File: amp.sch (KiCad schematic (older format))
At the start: 26 parts, among them IC1 STM32F103CBU6, IC2 MCP1700, J1 SERIAL, J2 MICROUSB, P1 SWD_TC, P2 SWD, Q1 PFET, Y1 8MHz

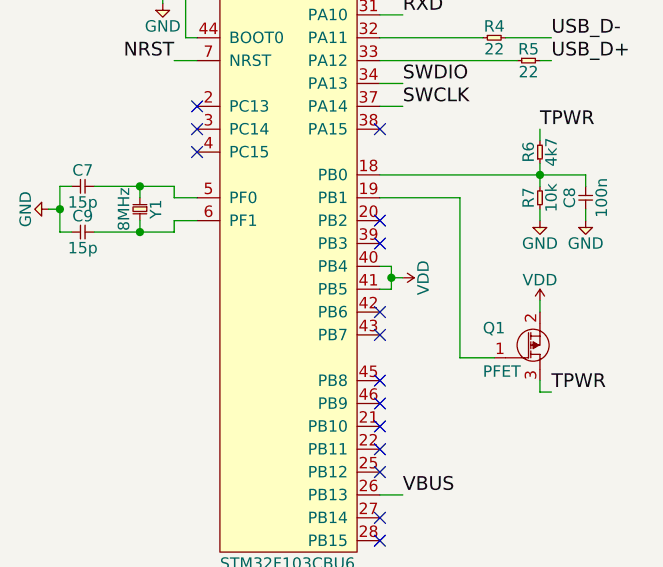
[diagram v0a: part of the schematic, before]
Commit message: Only need PB5 for version sensing
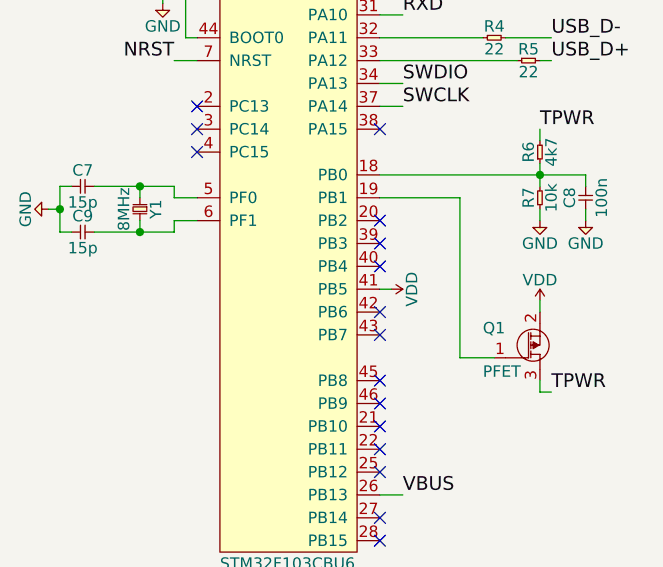
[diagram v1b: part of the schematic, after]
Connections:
- net VDD: no longer IC1.40 (PB4)
- no-connect marks 21 -> 22
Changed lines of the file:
@@
 L VDD #PWR017
 U 1 1 5686983C
-P 3650 4800
-F 0 "#PWR017" H 3650 4910 50  0001 L CNN
-F 1 "VDD" H 3650 4890 50  0000 C CNN
-F 2 "" H 3650 4800 60  0000 C CNN
-F 3 "" H 3650 4800 60  0000 C CNN
-	1    3650 4800
+P 3600 4850
+F 0 "#PWR017" H 3600 4960 50  0001 L CNN
+F 1 "VDD" H 3600 4940 50  0000 C CNN
+F 2 "" H 3600 4850 60  0000 C CNN
+F 3 "" H 3600 4850 60  0000 C CNN
+	1    3600 4850
 	0    1    1    0
 $EndComp
@@
 	3550 4450 3900 4450
 Wire Wire Line
-	3550 4750 3600 4750
-Wire Wire Line
-	3600 4750 3600 4850
-Wire Wire Line
 	3600 4850 3550 4850
-Wire Wire Line
-	3600 4800 3650 4800
-Connection ~ 3600 4800
 Wire Wire Line
 	3250 700  3250 750
@@
 	4250 1700 4250 1650
 Connection ~ 4150 1700
+NoConn ~ 3550 4750
 $EndSCHEMATC

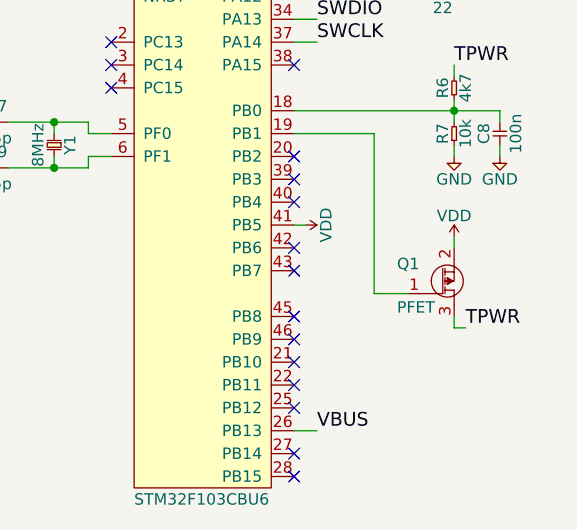
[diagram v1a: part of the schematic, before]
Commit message: Specify the PFET
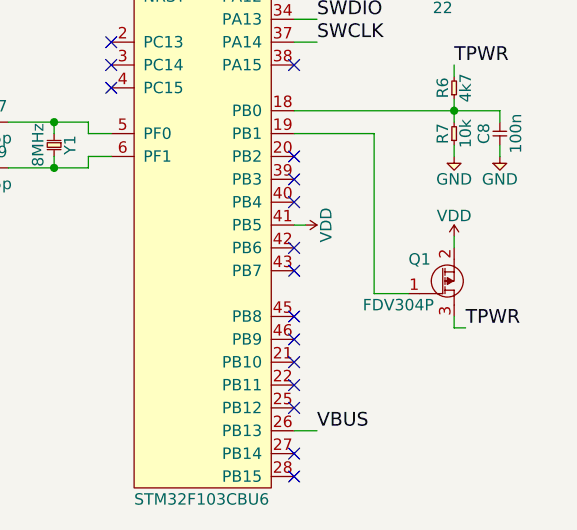
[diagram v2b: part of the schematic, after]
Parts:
- Q1: value PFET -> FDV304P; footprint (none) -> agg:SOT-23; Farnell (none) -> 9846123
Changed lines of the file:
@@
 U 1 1 56864DEA
 P 4250 5050
-F 0 "Q1" H 4000 5080 50  0000 L CNN
-F 1 "PFET" H 4000 4890 50  0000 L CNN
-F 2 "" H 4250 5050 60  0000 C CNN
+F 0 "Q1" H 4050 5100 50  0000 L CNN
+F 1 "FDV304P" H 3850 4900 50  0000 L CNN
+F 2 "agg:SOT-23" H 4250 5050 60  0001 C CNN
 F 3 "" H 4250 5050 60  0000 C CNN
+F 4 "9846123" H 4250 5050 60  0001 C CNN "Farnell"
 	1    4250 5050
 	1    0    0    -1

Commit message: mostly routed go
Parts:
- C1, C10, C11, C2: footprint agg:0603N -> agg:0603
- C3, C4, C5, C6, C8: footprint agg:0402N -> agg:0402
- C7, C9, R1, R2, R3, R4, R5, R6, R7: footprint (none) -> agg:0402
- IC1: Farnell (none) -> 2060891; Field4 2060891 -> (none)
- J1: footprint (none) -> agg:SM04B-PASS
- Y1: footprint (none) -> agg:XTAL-50x32; Farnell (none) -> 2101329
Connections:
- net GND: now also C1.1, C2.1, C3.1, C4.1, C5.1, C6.1
- net VDD: no longer C1.1, C2.1, C3.1, C4.1, C5.1, C6.1
- net STM32_D-: now reaches IC1.32 (PA11), R4.1
- net STM32_D+: now reaches IC1.33 (PA12), R5.1
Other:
- moved on the sheet: C1, C2, C3, C4, C5, C6
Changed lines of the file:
@@
 F 2 "agg:QFN-48-EP-ST" H 2850 2350 50  0001 L CNN
 F 3 "http://www.st.com/st-web-ui/static/active/en/resource/technical/document/datasheet/CD00161566.pdf" H 2850 2250 50  0001 L CNN
-F 4 "2060891" H 2850 2150 50  0001 L CNN "Field4"
+F 4 "2060891" H 3150 4250 60  0001 C CNN "Farnell"
 	1    3150 4250
 	1    0    0    -1
@@
 F 0 "J1" H 2350 650 50  0000 L CNN
 F 1 "SERIAL" V 2300 900 50  0000 C CNN
-F 2 "" H 2400 1050 60  0000 C CNN
+F 2 "agg:SM04B-PASS" H 2400 1050 60  0001 C CNN
 F 3 "" H 2400 1050 60  0000 C CNN
 	1    2400 1050
@@
 F 0 "R4" H 4050 3800 50  0000 C CNN
 F 1 "22" H 4050 3700 50  0000 C CNN
-F 2 "" H 4000 3750 60  0000 C CNN
+F 2 "agg:0402" H 4000 3750 60  0001 C CNN
 F 3 "" H 4000 3750 60  0000 C CNN
 	1    4000 3750
@@
 F 0 "R5" H 4200 3900 50  0000 C CNN
 F 1 "22" H 4200 3800 50  0000 C CNN
-F 2 "" H 4150 3850 60  0000 C CNN
+F 2 "agg:0402" H 4150 3850 60  0001 C CNN
 F 3 "" H 4150 3850 60  0000 C CNN
 	1    4150 3850
@@
 F 0 "R3" H 4100 3500 50  0000 C CNN
 F 1 "1k5" H 4100 3400 50  0000 C CNN
-F 2 "" H 4050 3450 60  0000 C CNN
+F 2 "agg:0402" H 4050 3450 60  0001 C CNN
 F 3 "" H 4050 3450 60  0000 C CNN
 	1    4050 3450
@@
 F 0 "R1" H 2200 1600 50  0000 C CNN
 F 1 "4k7" H 2200 1500 50  0000 C CNN
-F 2 "" H 2150 1550 60  0000 C CNN
+F 2 "agg:0402" H 2150 1550 60  0001 C CNN
 F 3 "" H 2150 1550 60  0000 C CNN
 	1    2150 1550
@@
 F 0 "R2" H 2200 1800 50  0000 C CNN
 F 1 "10k" H 2200 1700 50  0000 C CNN
-F 2 "" H 2150 1750 60  0000 C CNN
+F 2 "agg:0402" H 2150 1750 60  0001 C CNN
 F 3 "" H 2150 1750 60  0000 C CNN
 	1    2150 1750
@@
 F 0 "Y1" H 2550 4520 50  0000 C CNN
 F 1 "8MHz" H 2550 4380 50  0000 C CNN
-F 2 "" H 2500 4450 60  0000 C CNN
+F 2 "agg:XTAL-50x32" H 2500 4450 60  0001 C CNN
 F 3 "" H 2500 4450 60  0000 C CNN
+F 4 "2101329" H 2500 4450 50  0001 L CNN "Farnell"
 	1    2500 4450
 	0    1    1    0
@@
 F 0 "C7" H 2250 4470 50  0000 C CNN
 F 1 "15p" H 2250 4330 50  0000 C CNN
-F 2 "" H 2200 4400 60  0000 C CNN
+F 2 "agg:0402" H 2200 4400 60  0001 C CNN
 F 3 "" H 2200 4400 60  0000 C CNN
 	1    2200 4400
@@
 F 0 "C9" H 2250 4670 50  0000 C CNN
 F 1 "15p" H 2250 4530 50  0000 C CNN
-F 2 "" H 2200 4600 60  0000 C CNN
+F 2 "agg:0402" H 2200 4600 60  0001 C CNN
 F 3 "" H 2200 4600 60  0000 C CNN
 	1    2200 4600
@@
 L C C5
 U 1 1 56866C90
-P 2250 2750
-F 0 "C5" H 2300 2820 50  0000 C CNN
-F 1 "100n" H 2300 2680 50  0000 C CNN
-F 2 "agg:0402N" H 2250 2750 60  0001 C CNN
-F 3 "" H 2250 2750 60  0000 C CNN
-	1    2250 2750
+P 2150 3000
+F 0 "C5" H 2200 3070 50  0000 C CNN
+F 1 "100n" H 2200 2930 50  0000 C CNN
+F 2 "agg:0402" H 2150 3000 60  0001 C CNN
+F 3 "" H 2150 3000 60  0000 C CNN
+	1    2150 3000
 	0    -1   -1   0
 $EndComp
@@
 L C C4
 U 1 1 56866F6D
-P 2000 2750
-F 0 "C4" H 2050 2820 50  0000 C CNN
-F 1 "100n" H 2050 2680 50  0000 C CNN
-F 2 "agg:0402N" H 2000 2750 60  0001 C CNN
-F 3 "" H 2000 2750 60  0000 C CNN
-	1    2000 2750
+P 1900 2900
+F 0 "C4" H 1950 2970 50  0000 C CNN
+F 1 "100n" H 1950 2830 50  0000 C CNN
+F 2 "agg:0402" H 1900 2900 60  0001 C CNN
+F 3 "" H 1900 2900 60  0000 C CNN
+	1    1900 2900
 	0    -1   -1   0
 $EndComp
@@
 L C C3
 U 1 1 56866FB0
-P 1750 2750
-F 0 "C3" H 1800 2820 50  0000 C CNN
-F 1 "100n" H 1800 2680 50  0000 C CNN
-F 2 "agg:0402N" H 1750 2750 60  0001 C CNN
-F 3 "" H 1750 2750 60  0000 C CNN
-	1    1750 2750
+P 1650 2800
+F 0 "C3" H 1700 2870 50  0000 C CNN
+F 1 "100n" H 1700 2730 50  0000 C CNN
+F 2 "agg:0402" H 1650 2800 60  0001 C CNN
+F 3 "" H 1650 2800 60  0000 C CNN
+	1    1650 2800
 	0    -1   -1   0
 $EndComp
@@
 L C C6
 U 1 1 56867348
-P 2500 2750
-F 0 "C6" H 2550 2820 50  0000 C CNN
-F 1 "10n" H 2550 2680 50  0000 C CNN
-F 2 "agg:0402N" H 2500 2750 60  0001 C CNN
-F 3 "" H 2500 2750 60  0000 C CNN
-	1    2500 2750
+P 2600 3100
+F 0 "C6" H 2650 3170 50  0000 C CNN
+F 1 "10n" H 2650 3030 50  0000 C CNN
+F 2 "agg:0402" H 2600 3100 60  0001 C CNN
+F 3 "" H 2600 3100 60  0000 C CNN
+	1    2600 3100
 	0    -1   -1   0
 $EndComp
@@
 L C C2
 U 1 1 568673BC
-P 1500 2750
-F 0 "C2" H 1550 2800 50  0000 C CNN
-F 1 "1µ" H 1550 2680 50  0000 C CNN
-F 2 "agg:0603N" H 1500 2750 60  0001 C CNN
-F 3 "" H 1500 2750 60  0000 C CNN
-	1    1500 2750
+P 2350 3100
+F 0 "C2" H 2400 3150 50  0000 C CNN
+F 1 "1µ" H 2400 3030 50  0000 C CNN
+F 2 "agg:0603" H 2350 3100 60  0001 C CNN
+F 3 "" H 2350 3100 60  0000 C CNN
+	1    2350 3100
 	0    -1   -1   0
 $EndComp
@@
 L C C1
 U 1 1 5686747A
-P 1250 2750
-F 0 "C1" H 1300 2820 50  0000 C CNN
-F 1 "4µ7" H 1300 2680 50  0000 C CNN
-F 2 "agg:0603N" H 1250 2750 60  0001 C CNN
-F 3 "" H 1250 2750 60  0000 C CNN
-	1    1250 2750
+P 1400 2800
+F 0 "C1" H 1450 2870 50  0000 C CNN
+F 1 "4µ7" H 1450 2730 50  0000 C CNN
+F 2 "agg:0603" H 1400 2800 60  0001 C CNN
+F 3 "" H 1400 2800 60  0000 C CNN
+	1    1400 2800
 	0    -1   -1   0
 $EndComp
@@
 F 0 "R6" H 4300 4350 50  0000 C CNN
 F 1 "4k7" H 4300 4250 50  0000 C CNN
-F 2 "" H 4250 4300 60  0000 C CNN
+F 2 "agg:0402" H 4250 4300 60  0001 C CNN
 F 3 "" H 4250 4300 60  0000 C CNN
 	1    4250 4300
@@
 F 0 "R7" H 4300 4550 50  0000 C CNN
 F 1 "10k" H 4300 4450 50  0000 C CNN
-F 2 "" H 4250 4500 60  0000 C CNN
+F 2 "agg:0402" H 4250 4500 60  0001 C CNN
 F 3 "" H 4250 4500 60  0000 C CNN
 	1    4250 4500
@@
 F 0 "C8" H 4500 4570 50  0000 C CNN
 F 1 "100n" H 4500 4430 50  0000 C CNN
-F 2 "agg:0402N" H 4450 4500 60  0001 C CNN
+F 2 "agg:0402" H 4450 4500 60  0001 C CNN
 F 3 "" H 4450 4500 60  0000 C CNN
 	1    4450 4500
@@
 F 0 "C11" H 4200 1920 50  0000 C CNN
 F 1 "1µ" H 4200 1780 50  0000 C CNN
-F 2 "agg:0603N" H 4150 1850 60  0001 C CNN
+F 2 "agg:0603" H 4150 1850 60  0001 C CNN
 F 3 "" H 4150 1850 60  0000 C CNN
 	1    4150 1850
@@
 F 0 "C10" H 3100 1920 50  0000 C CNN
 F 1 "1µ" H 3100 1780 50  0000 C CNN
-F 2 "agg:0603N" H 3050 1850 60  0001 C CNN
+F 2 "agg:0603" H 3050 1850 60  0001 C CNN
 F 3 "" H 3050 1850 60  0000 C CNN
 	1    3050 1850
 	0    -1   -1   0
 $EndComp
+NoConn ~ 3550 4750
 Wire Wire Line
 	3550 3950 3650 3950
@@
 	2650 3850 2750 3850
 Wire Wire Line
-	2750 3150 2600 3150
-Wire Wire Line
-	2600 3150 2600 3600
-Wire Wire Line
-	2750 3250 2600 3250
+	2600 3100 2600 3600
+Wire Wire Line
+	1400 3250 2750 3250
 Connection ~ 2600 3250
 Wire Wire Line
-	2750 3350 2600 3350
+	1900 3350 2750 3350
 Connection ~ 2600 3350
 Wire Wire Line
-	2750 3450 2600 3450
+	2150 3450 2750 3450
 Connection ~ 2600 3450
 Wire Wire Line
@@
 Wire Wire Line
 	2700 2500 2700 2950
-Wire Wire Line
-	1250 2950 2750 2950
-Wire Wire Line
-	2750 2850 2700 2850
 Connection ~ 2700 2850
-Wire Wire Line
-	2750 2750 2700 2750
 Connection ~ 2700 2750
 Wire Wire Line
-	2750 2650 2700 2650
+	1400 2650 2750 2650
 Connection ~ 2700 2650
-Wire Wire Line
-	1250 2550 2750 2550
 Connection ~ 2700 2550
-Wire Wire Line
-	2500 2750 2500 2950
-Connection ~ 2700 2950
-Wire Wire Line
-	1250 2950 1250 2750
-Connection ~ 2500 2950
-Wire Wire Line
-	1500 2750 1500 2950
-Connection ~ 1500 2950
-Wire Wire Line
-	1750 2750 1750 2950
-Connection ~ 1750 2950
-Wire Wire Line
-	2000 2750 2000 2950
-Connection ~ 2000 2950
-Wire Wire Line
-	2250 2750 2250 2950
-Connection ~ 2250 2950
-Wire Wire Line
-	1250 2650 1250 2550
-Wire Wire Line
-	2500 2650 2500 2550
-Connection ~ 2500 2550
-Wire Wire Line
-	2250 2650 2250 2550
-Connection ~ 2250 2550
-Wire Wire Line
-	2000 2650 2000 2550
-Connection ~ 2000 2550
-Wire Wire Line
-	1750 2650 1750 2550
-Connection ~ 1750 2550
-Wire Wire Line
-	1500 2650 1500 2550
-Connection ~ 1500 2550
 Wire Wire Line
 	4400 1150 4300 1150
@@
 	4250 1700 4250 1650
 Connection ~ 4150 1700
-NoConn ~ 3550 4750
+Wire Wire Line
+	2350 2950 2750 2950
+Wire Wire Line
+	2350 3150 2750 3150
+Wire Wire Line
+	2750 2550 2700 2550
+Wire Wire Line
+	2600 2950 2600 3000
+Connection ~ 2700 2950
+Wire Wire Line
+	2350 2950 2350 3000
+Connection ~ 2600 2950
+Connection ~ 2600 3150
+Wire Wire Line
+	2350 3100 2350 3150
+Wire Wire Line
+	1650 2650 1650 2700
+Wire Wire Line
+	1400 2650 1400 2700
+Connection ~ 1650 2650
+Wire Wire Line
+	2750 2850 2150 2850
+Wire Wire Line
+	2150 2850 2150 2900
+Wire Wire Line
+	2750 2750 1900 2750
+Wire Wire Line
+	1900 2750 1900 2800
+Wire Wire Line
+	2150 3000 2150 3450
+Wire Wire Line
+	1900 2900 1900 3350
+Wire Wire Line
+	1650 2800 1650 3250
+Wire Wire Line
+	1400 2800 1400 3250
+Connection ~ 1650 3250
+Text Label 3550 3750 0    30   ~ 0
+STM32_D-
+Text Label 3550 3850 0    30   ~ 0
+STM32_D+
 $EndSCHEMATC

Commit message: fully routed
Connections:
- net GND: now also J1.4; no longer J1.1
- net RXD: now also J1.3; no longer J1.2
- net TXD: now also J1.2; no longer J1.3
- net VDD: now also J1.1; no longer J1.4
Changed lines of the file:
@@
 L CONN_01x04 J1
 U 1 1 568643A2
-P 2400 1050
-F 0 "J1" H 2350 650 50  0000 L CNN
-F 1 "SERIAL" V 2300 900 50  0000 C CNN
-F 2 "agg:SM04B-PASS" H 2400 1050 60  0001 C CNN
-F 3 "" H 2400 1050 60  0000 C CNN
-	1    2400 1050
-	1    0    0    1
+P 2400 750
+F 0 "J1" H 2350 350 50  0000 L CNN
+F 1 "SERIAL" V 2300 600 50  0000 C CNN
+F 2 "agg:SM04B-PASS" H 2400 750 60  0001 C CNN
+F 3 "" H 2400 750 60  0000 C CNN
+	1    2400 750
+	1    0    0    -1
 $EndComp
 Text Label 3650 3950 0    60   ~ 0

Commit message: try swap to surface-mount swd connector
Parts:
- P2: footprint agg:FTSH-105-01-F-D-K -> agg:FTSH-105-01-L-DV-K; Toby FTSH-105-01-F-D-K -> agg:FTSH-105-01-L-DV-K
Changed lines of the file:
@@
 F 0 "P2" H 3400 1250 50  0000 L CNN
 F 1 "SWD" H 3400 650 50  0000 L CNN
-F 2 "agg:FTSH-105-01-F-D-K" H 3400 550 50  0001 L CNN
+F 2 "agg:FTSH-105-01-L-DV-K" H 3400 550 50  0001 L CNN
 F 3 "" H 4150 750 50  0000 C CNN
-F 4 "FTSH-105-01-F-D-K" H 3400 450 50  0001 L CNN "Toby"
+F 4 "agg:FTSH-105-01-L-DV-K" H 3400 450 50  0001 L CNN "Toby"
 	1    3800 950
 	1    0    0    -1

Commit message: Add Farnell order codes
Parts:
- C1: Farnell (none) -> 2496930
- C10, C11, C2: Farnell (none) -> 2496916
- C3, C4, C5, C8: Farnell (none) -> 1759380
- C6: Farnell (none) -> 1758924
- C7, C9: value 15p -> 33p; Farnell (none) -> 1758955
- J1: Farnell (none) -> 2399347
- P2: Toby agg:FTSH-105-01-L-DV-K -> FTSH-105-01-L-DV-K
- R1, R6: Farnell (none) -> 2447187
- R2, R7: Farnell (none) -> 2447096
- R3: Farnell (none) -> 2447125
- R4, R5: Farnell (none) -> 2447138
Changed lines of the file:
@@
 F 2 "agg:FTSH-105-01-L-DV-K" H 3400 550 50  0001 L CNN
 F 3 "" H 4150 750 50  0000 C CNN
-F 4 "agg:FTSH-105-01-L-DV-K" H 3400 450 50  0001 L CNN "Toby"
+F 4 "FTSH-105-01-L-DV-K" H 3400 450 50  0001 L CNN "Toby"
 	1    3800 950
 	1    0    0    -1
@@
 F 2 "agg:SM04B-PASS" H 2400 750 60  0001 C CNN
 F 3 "" H 2400 750 60  0000 C CNN
+F 4 "2399347" H 2400 750 60  0001 C CNN "Farnell"
 	1    2400 750
 	1    0    0    -1
@@
 F 2 "agg:0402" H 4000 3750 60  0001 C CNN
 F 3 "" H 4000 3750 60  0000 C CNN
+F 4 "2447138" H 4000 3750 60  0001 C CNN "Farnell"
 	1    4000 3750
 	1    0    0    -1
@@
 F 2 "agg:0402" H 4150 3850 60  0001 C CNN
 F 3 "" H 4150 3850 60  0000 C CNN
+F 4 "2447138" H 4150 3850 60  0001 C CNN "Farnell"
 	1    4150 3850
 	1    0    0    -1
@@
 F 2 "agg:0402" H 4050 3450 60  0001 C CNN
 F 3 "" H 4050 3450 60  0000 C CNN
+F 4 "2447125" H 4050 3450 60  0001 C CNN "Farnell"
 	1    4050 3450
 	1    0    0    -1
@@
 F 2 "agg:0402" H 2150 1550 60  0001 C CNN
 F 3 "" H 2150 1550 60  0000 C CNN
+F 4 "2447187" H 2150 1550 60  0001 C CNN "Farnell"
 	1    2150 1550
 	0    -1   -1   0
@@
 F 2 "agg:0402" H 2150 1750 60  0001 C CNN
 F 3 "" H 2150 1750 60  0000 C CNN
+F 4 "2447096" H 2150 1750 60  0001 C CNN "Farnell"
 	1    2150 1750
 	0    -1   -1   0
@@
 P 2200 4400
 F 0 "C7" H 2250 4470 50  0000 C CNN
-F 1 "15p" H 2250 4330 50  0000 C CNN
+F 1 "33p" H 2250 4330 50  0000 C CNN
 F 2 "agg:0402" H 2200 4400 60  0001 C CNN
 F 3 "" H 2200 4400 60  0000 C CNN
+F 4 "1758955" H 2200 4400 60  0001 C CNN "Farnell"
 	1    2200 4400
 	1    0    0    -1
@@
 P 2200 4600
 F 0 "C9" H 2250 4670 50  0000 C CNN
-F 1 "15p" H 2250 4530 50  0000 C CNN
+F 1 "33p" H 2250 4530 50  0000 C CNN
 F 2 "agg:0402" H 2200 4600 60  0001 C CNN
 F 3 "" H 2200 4600 60  0000 C CNN
+F 4 "1758955" H 2200 4600 60  0001 C CNN "Farnell"
 	1    2200 4600
 	1    0    0    -1
@@
 F 2 "agg:0402" H 2150 3000 60  0001 C CNN
 F 3 "" H 2150 3000 60  0000 C CNN
+F 4 "1759380" H 2150 3000 60  0001 C CNN "Farnell"
 	1    2150 3000
 	0    -1   -1   0
@@
 F 2 "agg:0402" H 1900 2900 60  0001 C CNN
 F 3 "" H 1900 2900 60  0000 C CNN
+F 4 "1759380" H 1900 2900 60  0001 C CNN "Farnell"
 	1    1900 2900
 	0    -1   -1   0
@@
 F 2 "agg:0402" H 1650 2800 60  0001 C CNN
 F 3 "" H 1650 2800 60  0000 C CNN
+F 4 "1759380" H 1650 2800 60  0001 C CNN "Farnell"
 	1    1650 2800
 	0    -1   -1   0
@@
 F 2 "agg:0402" H 2600 3100 60  0001 C CNN
 F 3 "" H 2600 3100 60  0000 C CNN
+F 4 "1758924" H 2600 3100 60  0001 C CNN "Farnell"
 	1    2600 3100
 	0    -1   -1   0
@@
 F 2 "agg:0603" H 2350 3100 60  0001 C CNN
 F 3 "" H 2350 3100 60  0000 C CNN
+F 4 "2496916" H 2350 3100 60  0001 C CNN "Farnell"
 	1    2350 3100
 	0    -1   -1   0
@@
 F 2 "agg:0603" H 1400 2800 60  0001 C CNN
 F 3 "" H 1400 2800 60  0000 C CNN
+F 4 "2496930" H 1400 2800 60  0001 C CNN "Farnell"
 	1    1400 2800
 	0    -1   -1   0
@@
 F 2 "agg:0402" H 4250 4300 60  0001 C CNN
 F 3 "" H 4250 4300 60  0000 C CNN
+F 4 "2447187" H 4250 4300 60  0001 C CNN "Farnell"
 	1    4250 4300
 	0    -1   -1   0
@@
 F 2 "agg:0402" H 4250 4500 60  0001 C CNN
 F 3 "" H 4250 4500 60  0000 C CNN
+F 4 "2447096" H 4250 4500 60  0001 C CNN "Farnell"
 	1    4250 4500
 	0    -1   -1   0
@@
 F 2 "agg:0402" H 4450 4500 60  0001 C CNN
 F 3 "" H 4450 4500 60  0000 C CNN
+F 4 "1759380" H 4450 4500 60  0001 C CNN "Farnell"
 	1    4450 4500
 	0    -1   -1   0
@@
 F 2 "agg:0603" H 4150 1850 60  0001 C CNN
 F 3 "" H 4150 1850 60  0000 C CNN
+F 4 "2496916" H 4150 1850 60  0001 C CNN "Farnell"
 	1    4150 1850
 	0    -1   -1   0
@@
 F 2 "agg:0603" H 3050 1850 60  0001 C CNN
 F 3 "" H 3050 1850 60  0000 C CNN
+F 4 "2496916" H 3050 1850 60  0001 C CNN "Farnell"
 	1    3050 1850
 	0    -1   -1   0
